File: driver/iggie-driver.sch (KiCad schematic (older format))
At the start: 1 part, among them J101 HV

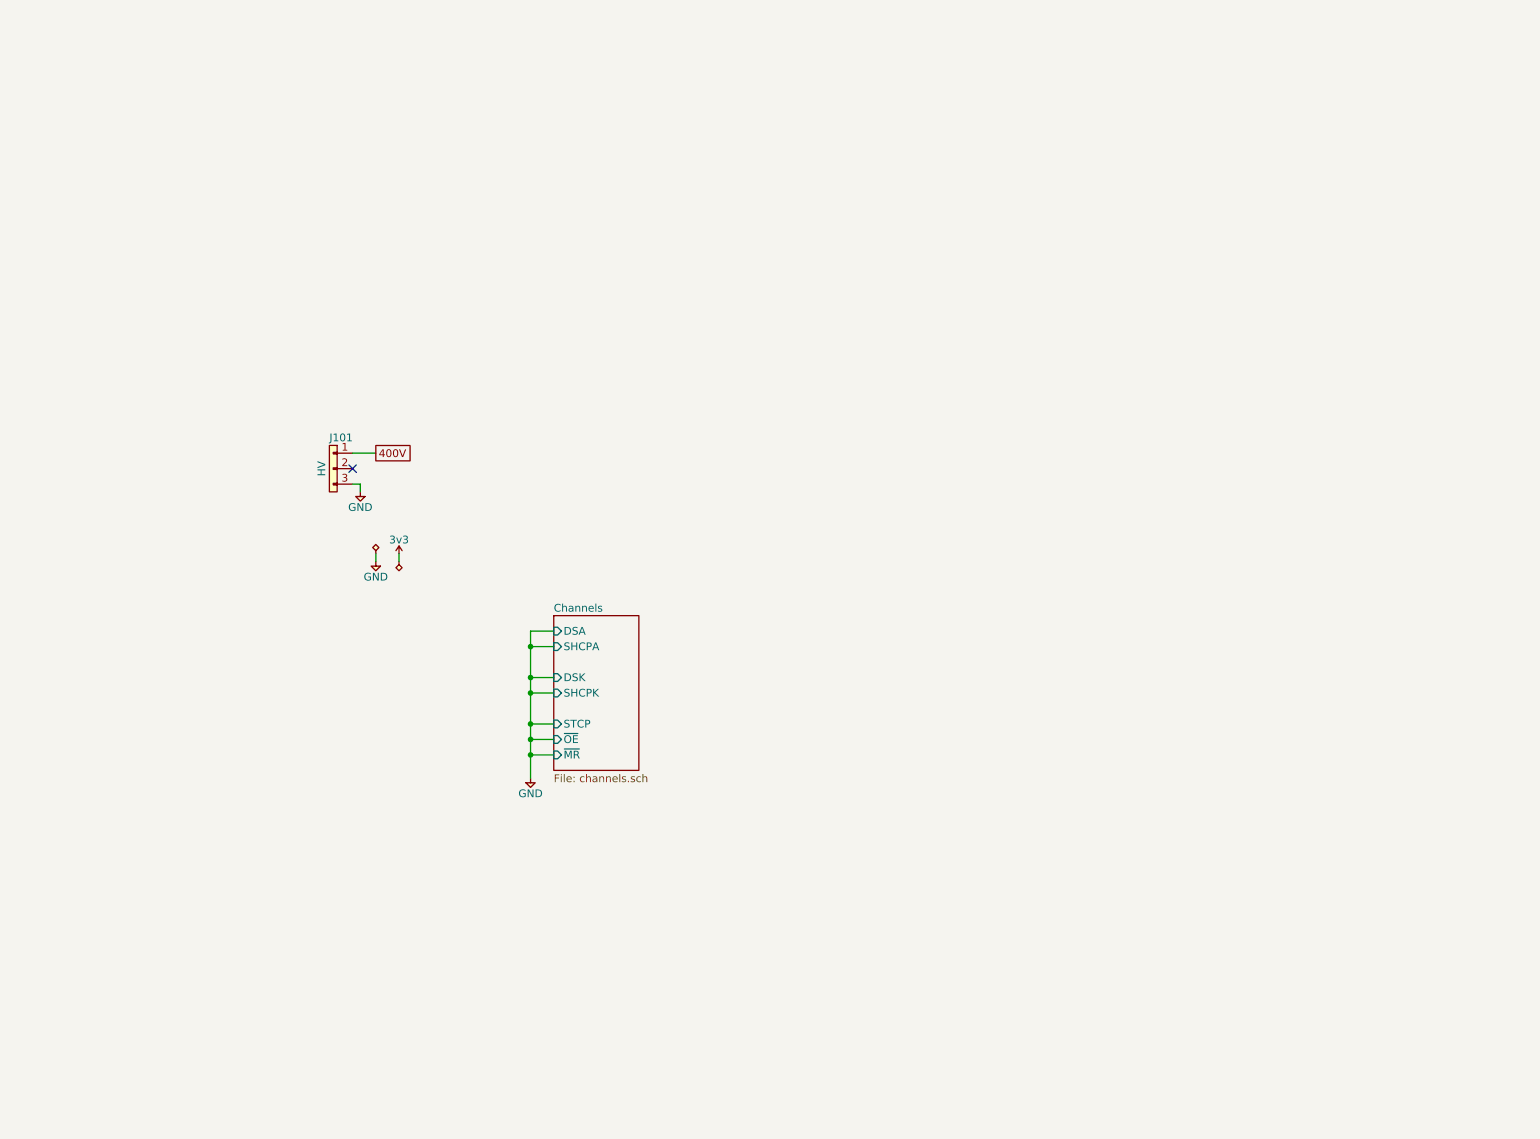
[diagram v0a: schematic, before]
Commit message: Finish sch, start PCB
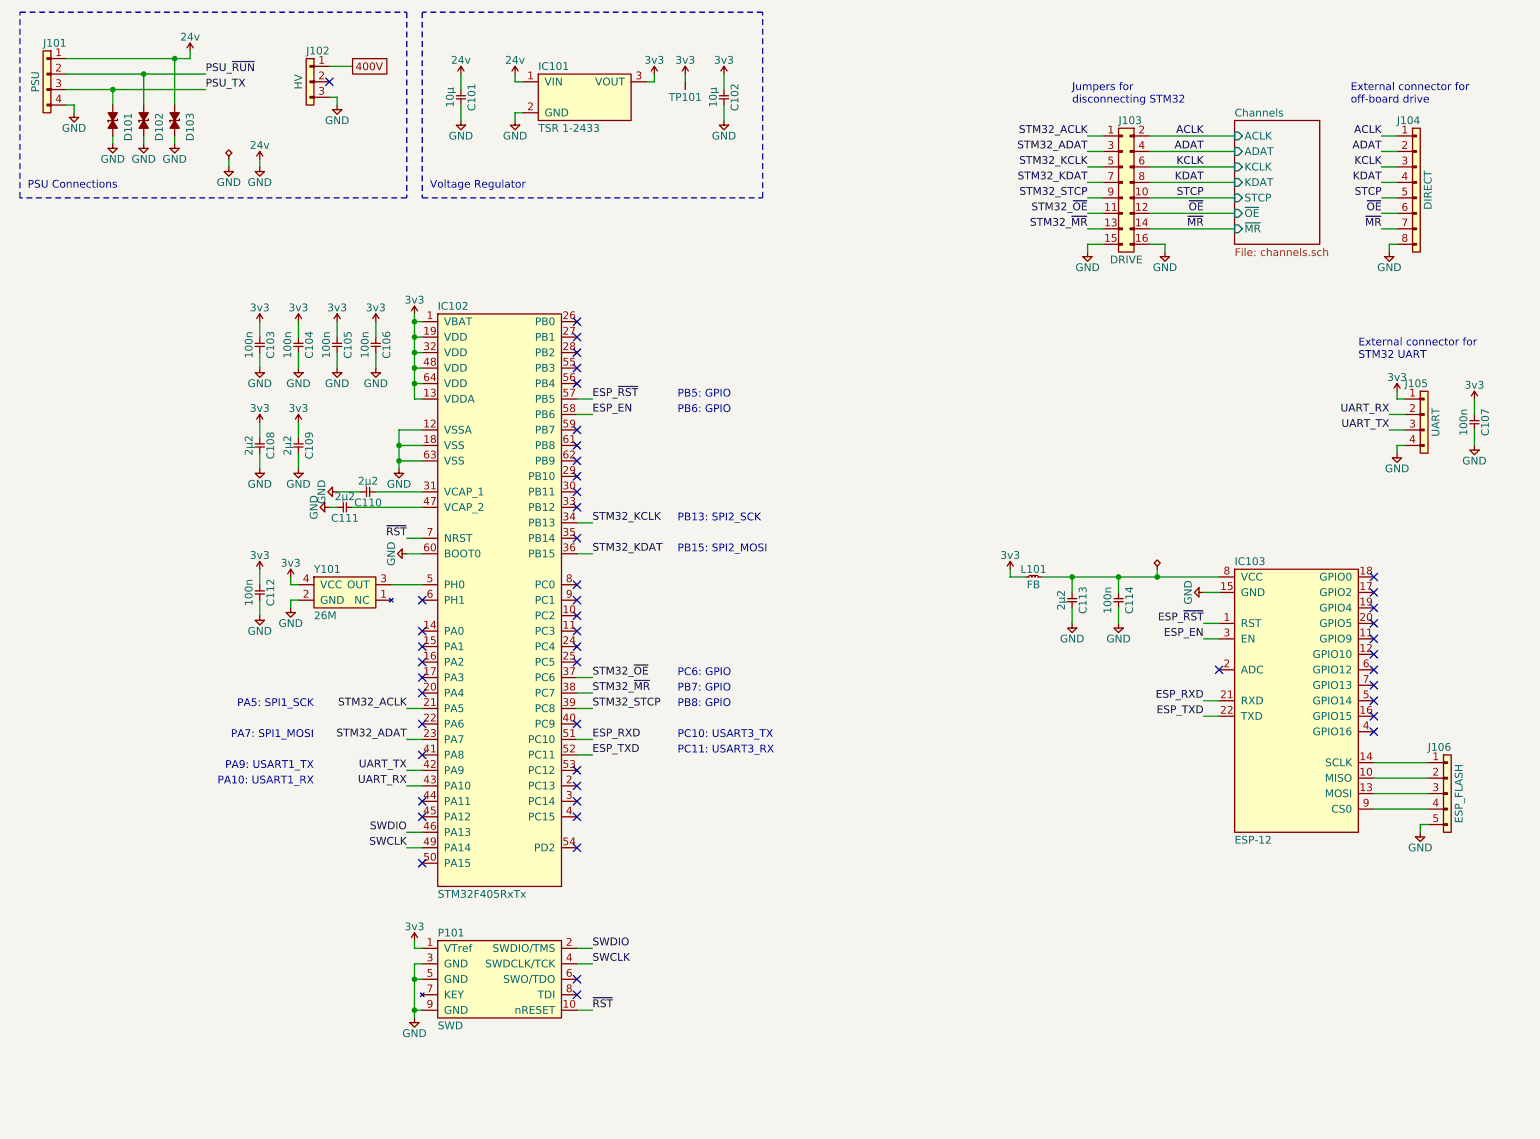
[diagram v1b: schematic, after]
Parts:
- added C101, C102: 10µ, agg:1210, symbol agg-kicad:C
- added C103, C104, C105, C106, C107, C112, C114: 100n, agg:0603, symbol agg-kicad:C
- added C108, C109, C110, C111, C113: 2µ2, agg:0603, symbol agg-kicad:C
- added D101, D102, D103: ESD_DIODE, agg:0603, symbol agg-kicad:ESD_DIODE
- added IC101: TSR 1-2433, agg:TSR1, symbol agg-kicad:TSR1
- added IC102: STM32F405RxTx, agg:LQFP-64, symbol agg-kicad:STM32F405RxTx
- added IC103: ESP-12, agg:ESP-12, symbol agg-kicad:ESP-12
- added J101: PSU, agg:MOLEX-KK-254P-04, symbol agg-kicad:CONN_01x04
- added J103: DRIVE, agg:DIL-254P-16, symbol agg-kicad:CONN_02x08
- added J104: DIRECT, agg:MOLEX-PICOBLADE-53398-0871, symbol agg-kicad:CONN_01x08
- added J105: UART, agg:MOLEX-PICOBLADE-53398-0471, symbol agg-kicad:CONN_01x04
- added J106: ESP_FLASH, agg:SIL-254P-05, symbol agg-kicad:CONN_01x05
- added L101: FB, agg:0603, symbol agg-kicad:L
- added P101: SWD, agg:FTSH-105-01-F-D-K, symbol agg-kicad:SWD
- added TP101: TESTPAD, agg:TESTPAD, symbol agg-kicad:TESTPAD
- added Y101: 26M, agg:XTAL-25x20, symbol agg-kicad:TCXO
- J102: renamed from J101; footprint (none) -> agg:MOLEX-KK-254P-03; Farnell (none) -> 1360131
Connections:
- net 3v3: now also C102.1, C103.1, C104.1, C105.1, C106.1, C107.1, C108.1, C109.1, C112.1, IC101.3 (VOUT), IC102.1 (VBAT), IC102.13 (VDDA), IC102.19 (VDD), IC102.32 (VDD), IC102.48 (VDD), IC102.64 (VDD), J105.1, L101.1, P101.1 (VTref), TP101.1 (TP), Y101.4 (VCC)
- net GND renamed 24v
- net 24v: now also C101.1, C101.2, C102.2, C103.2, C104.2, C105.2, C106.2, C107.2, C108.2, C109.2, C110.2, C111.2, C112.2, C113.2, C114.2, D101.2, D102.2, D103.1, D103.2, IC101.1 (VIN), IC101.2 (GND), IC102.12 (VSSA), IC102.18 (VSS), IC102.60 (BOOT0), IC102.63 (VSS), IC103.15 (GND), J101.1, J101.4, J103.15, J103.16, J104.8, J105.4, J106.5, P101.3 (GND), P101.5 (GND), P101.9 (GND), Y101.2 (GND)
- new net: C110.1, IC102.31 (VCAP_1)
- new net: C111.1, IC102.47 (VCAP_2)
- new net: IC102.5 (PH0), Y101.3 (OUT)
- new net: IC103.10 (MISO), J106.2
- new net: IC103.13 (MOSI), J106.3
- new net: IC103.14 (SCLK), J106.1
- new net: C113.1, C114.1, IC103.8 (VCC), L101.2
- new net: IC103.9 (CS0), J106.4
- new net ACLK: J103.2, J104.1
- new net ADAT: J103.4, J104.2
- new net ESP_EN: IC102.58 (PB6), IC103.3 (EN)
- new net ESP_RXD: IC102.51 (PC10), IC103.21 (RXD)
- new net ESP_TXD: IC102.52 (PC11), IC103.22 (TXD)
- new net ESP_~RST: IC102.57 (PB5), IC103.1 (RST)
- new net KCLK: J103.6, J104.3
- new net KDAT: J103.8, J104.4
- new net PSU_TX: D101.1, J101.3
- new net PSU_~RUN: D102.1, J101.2
- new net STCP: J103.10, J104.5
- new net STM32_ACLK: IC102.21 (PA5), J103.1
- new net STM32_ADAT: IC102.23 (PA7), J103.3
- new net STM32_KCLK: IC102.34 (PB13), J103.5
- new net STM32_KDAT: IC102.36 (PB15), J103.7
- new net STM32_STCP: IC102.39 (PC8), J103.9
- new net STM32_~MR: IC102.38 (PC7), J103.13
- new net STM32_~OE: IC102.37 (PC6), J103.11
- new net SWCLK: IC102.49 (PA14), P101.4 (SWDCLK/TCK)
- new net SWDIO: IC102.46 (PA13), P101.2 (SWDIO/TMS)
- new net UART_RX: IC102.43 (PA10), J105.2
- new net UART_TX: IC102.42 (PA9), J105.3
- new net ~MR: J103.14, J104.7
- new net ~OE: J103.12, J104.6
- new net ~RST: IC102.7 (NRST), P101.10 (nRESET)
- no-connect marks 1 -> 50
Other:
- note added: "External connector for\nSTM32 UART"
- note added: "External connector for\noff-board drive"
- note added: "Jumpers for\ndisconnecting STM32"
- note added: "PA10: USART1_RX"
- note added: "PA5: SPI1_SCK"
- note added: "PA7: SPI1_MOSI"
- note added: "PA9: USART1_TX"
- note added: "PB13: SPI2_SCK"
- note added: "PB15: SPI2_MOSI"
- note added: "PB5: GPIO"
- note added: "PB6: GPIO"
- note added: "PB7: GPIO"
- note added: "PB8: GPIO"
- note added: "PC10: USART3_TX"
- note added: "PC11: USART3_RX"
- note added: "PC6: GPIO"
- note added: "PSU Connections"
- note added: "Voltage Regulator"
- moved on the sheet: J102

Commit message: WIP PCB
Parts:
- added X101, X102, X103, X104, X105, X106, X107, X108: M3 MOUNT, agg:M3_MOUNT, symbol agg-kicad:PART
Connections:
- net 24v: no longer C101.2, C102.2, C103.2, C104.2, C105.2, C106.2, C107.2, C108.2, C109.2, C110.2, C111.2, C112.2, C113.2, C114.2, D101.2, D102.2, D103.2, IC101.2 (GND), IC102.12 (VSSA), IC102.18 (VSS), IC102.60 (BOOT0), IC102.63 (VSS), IC103.15 (GND), J101.4, J102.3, J103.15, J103.16, J104.8, J105.4, J106.5, P101.3 (GND), P101.5 (GND), P101.9 (GND), Y101.2 (GND)
- net 400V: now also J102.3; no longer J102.1
- net at IC103.10 (MISO): now also J106.3; no longer J106.2
- net at IC103.13 (MOSI): now also J106.2; no longer J106.3
- new net GND: C101.2, C102.2, C103.2, C104.2, C105.2, C106.2, C107.2, C108.2, C109.2, C110.2, C111.2, C112.2, C113.2, C114.2, D101.2, D102.2, D103.2, IC101.2 (GND), IC102.12 (VSSA), IC102.18 (VSS), IC102.60 (BOOT0), IC102.63 (VSS), IC103.15 (GND), J101.4, J102.1, J103.15, J103.16, J104.8, J105.4, J106.5, P101.3 (GND), P101.5 (GND), P101.9 (GND), Y101.2 (GND)
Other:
- moved on the sheet: J106
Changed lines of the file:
@@
 Comment4 ""
 $EndDescr
-$Comp
-L agg-kicad:CONN_01x03 J102
-U 1 1 5D894B24
-P 2450 900
-F 0 "J102" H 2400 1000 50  0000 L CNN
-F 1 "HV" V 2350 800 50  0000 C CNN
-F 2 "agg:MOLEX-KK-254P-03" H 2450 900 50  0001 C CNN
-F 3 "" H 2450 900 50  0001 C CNN
-F 4 "1360131" H 2450 900 50  0001 C CNN "Farnell"
-	1    2450 900
-	1    0    0    -1
-$EndComp
 NoConn ~ 2550 1000
 $Comp
@@
 	1    2100 1500
 	1    0    0    -1
-$EndComp
-$Comp
-L agg-kicad:GND #PWR0117
-U 1 1 8382BEE8
-P 2100 1550
-F 0 "#PWR0117" H 1970 1590 50  0001 L CNN
-F 1 "GND" H 2100 1450 50  0000 C CNN
-F 2 "" H 2100 1550 50  0001 C CNN
-F 3 "" H 2100 1550 50  0001 C CNN
-	1    2100 1550
-	-1   0    0    -1
 $EndComp
 Wire Wire Line
@@
 	1    0    0    -1
 $EndComp
-$Comp
-L agg-kicad:CONN_01x05 J106
-U 1 1 83A0715A
-P 9750 5400
-F 0 "J106" H 9700 5500 50  0000 L CNN
-F 1 "ESP_FLASH" V 9650 5200 50  0000 C CNN
-F 2 "agg:SIL-254P-05" H 9750 5400 50  0001 C CNN
-F 3 "" H 9750 5400 50  0001 C CNN
-	1    9750 5400
-	-1   0    0    -1
-$EndComp
-Wire Wire Line
-	9300 5400 9650 5400
-Wire Wire Line
-	9650 5500 9300 5500
-Wire Wire Line
-	9300 5600 9650 5600
-Wire Wire Line
-	9650 5700 9300 5700
-$Comp
-L agg-kicad:GND #PWR0150
-U 1 1 83A1A036
-P 9600 5850
-F 0 "#PWR0150" H 9470 5890 50  0001 L CNN
-F 1 "GND" H 9600 5750 50  0000 C CNN
-F 2 "" H 9600 5850 50  0001 C CNN
-F 3 "" H 9600 5850 50  0001 C CNN
-	1    9600 5850
-	1    0    0    -1
-$EndComp
-Wire Wire Line
-	9600 5850 9600 5800
-Wire Wire Line
-	9600 5800 9650 5800
 Wire Wire Line
 	8300 5000 8200 5000
@@
 Wire Wire Line
 	7900 4200 8300 4200
+$Comp
+L agg-kicad:PART X105
+U 1 1 83D5BB64
+P 500 7700
+F 0 "X105" H 550 7800 50  0000 L CNN
+F 1 "M3 MOUNT" H 550 7700 50  0000 L CNN
+F 2 "agg:M3_MOUNT" H 500 7700 50  0001 C CNN
+F 3 "" H 500 7700 50  0001 C CNN
+	1    500  7700
+	1    0    0    -1
+$EndComp
+$Comp
+L agg-kicad:PART X106
+U 1 1 83D5F3E2
+P 1050 7700
+F 0 "X106" H 1100 7800 50  0000 L CNN
+F 1 "M3 MOUNT" H 1100 7700 50  0000 L CNN
+F 2 "agg:M3_MOUNT" H 1050 7700 50  0001 C CNN
+F 3 "" H 1050 7700 50  0001 C CNN
+	1    1050 7700
+	1    0    0    -1
+$EndComp
+$Comp
+L agg-kicad:PART X107
+U 1 1 83D5F6EB
+P 1600 7700
+F 0 "X107" H 1650 7800 50  0000 L CNN
+F 1 "M3 MOUNT" H 1650 7700 50  0000 L CNN
+F 2 "agg:M3_MOUNT" H 1600 7700 50  0001 C CNN
+F 3 "" H 1600 7700 50  0001 C CNN
+	1    1600 7700
+	1    0    0    -1
+$EndComp
+$Comp
+L agg-kicad:PART X108
+U 1 1 83D5FB17
+P 2150 7700
+F 0 "X108" H 2200 7800 50  0000 L CNN
+F 1 "M3 MOUNT" H 2200 7700 50  0000 L CNN
+F 2 "agg:M3_MOUNT" H 2150 7700 50  0001 C CNN
+F 3 "" H 2150 7700 50  0001 C CNN
+	1    2150 7700
+	1    0    0    -1
+$EndComp
+$Comp
+L agg-kicad:PART X104
+U 1 1 83D5FDE9
+P 2150 7450
+F 0 "X104" H 2200 7550 50  0000 L CNN
+F 1 "M3 MOUNT" H 2200 7450 50  0000 L CNN
+F 2 "agg:M3_MOUNT" H 2150 7450 50  0001 C CNN
+F 3 "" H 2150 7450 50  0001 C CNN
+	1    2150 7450
+	1    0    0    -1
+$EndComp
+$Comp
+L agg-kicad:PART X103
+U 1 1 83D600CB
+P 1600 7450
+F 0 "X103" H 1650 7550 50  0000 L CNN
+F 1 "M3 MOUNT" H 1650 7450 50  0000 L CNN
+F 2 "agg:M3_MOUNT" H 1600 7450 50  0001 C CNN
+F 3 "" H 1600 7450 50  0001 C CNN
+	1    1600 7450
+	1    0    0    -1
+$EndComp
+$Comp
+L agg-kicad:PART X102
+U 1 1 83D6036C
+P 1050 7450
+F 0 "X102" H 1100 7550 50  0000 L CNN
+F 1 "M3 MOUNT" H 1100 7450 50  0000 L CNN
+F 2 "agg:M3_MOUNT" H 1050 7450 50  0001 C CNN
+F 3 "" H 1050 7450 50  0001 C CNN
+	1    1050 7450
+	1    0    0    -1
+$EndComp
+$Comp
+L agg-kicad:PART X101
+U 1 1 83D606DD
+P 500 7450
+F 0 "X101" H 550 7550 50  0000 L CNN
+F 1 "M3 MOUNT" H 550 7450 50  0000 L CNN
+F 2 "agg:M3_MOUNT" H 500 7450 50  0001 C CNN
+F 3 "" H 500 7450 50  0001 C CNN
+	1    500  7450
+	1    0    0    -1
+$EndComp
+$Comp
+L agg-kicad:PWR #FLG0103
+U 1 1 83D6639C
+P 2100 1550
+F 0 "#FLG0103" H 2100 1710 50  0001 C CNN
+F 1 "PWR" H 2100 1640 50  0001 C CNN
+F 2 "" H 2100 1550 50  0001 C CNN
+F 3 "" H 2100 1550 50  0001 C CNN
+	1    2100 1550
+	-1   0    0    1
+$EndComp
+$Comp
+L agg-kicad:CONN_01x03 J102
+U 1 1 5D894B24
+P 2450 1100
+F 0 "J102" H 2300 800 50  0000 L CNN
+F 1 "HV" V 2350 1000 50  0000 C CNN
+F 2 "agg:MOLEX-KK-254P-03" H 2450 1100 50  0001 C CNN
+F 3 "" H 2450 1100 50  0001 C CNN
+F 4 "1360131" H 2450 1100 50  0001 C CNN "Farnell"
+	1    2450 1100
+	1    0    0    1
+$EndComp
+$Comp
+L agg-kicad:CONN_01x05 J106
+U 1 1 83A0715A
+P 10000 5400
+F 0 "J106" H 9950 5500 50  0000 L CNN
+F 1 "ESP_FLASH" V 9900 5200 50  0000 C CNN
+F 2 "agg:SIL-254P-05" H 10000 5400 50  0001 C CNN
+F 3 "" H 10000 5400 50  0001 C CNN
+	1    10000 5400
+	-1   0    0    -1
+$EndComp
+Wire Wire Line
+	9300 5400 9900 5400
+Wire Wire Line
+	9900 5700 9300 5700
+$Comp
+L agg-kicad:GND #PWR0150
+U 1 1 83A1A036
+P 9850 5850
+F 0 "#PWR0150" H 9720 5890 50  0001 L CNN
+F 1 "GND" H 9850 5750 50  0000 C CNN
+F 2 "" H 9850 5850 50  0001 C CNN
+F 3 "" H 9850 5850 50  0001 C CNN
+	1    9850 5850
+	1    0    0    -1
+$EndComp
+Wire Wire Line
+	9850 5850 9850 5800
+Wire Wire Line
+	9850 5800 9900 5800
+Wire Wire Line
+	9300 5600 9600 5600
+Wire Wire Line
+	9600 5600 9600 5500
+Wire Wire Line
+	9600 5500 9900 5500
+Wire Wire Line
+	9300 5500 9450 5500
+Wire Wire Line
+	9450 5500 9450 5800
+Wire Wire Line
+	9450 5800 9750 5800
+Wire Wire Line
+	9750 5800 9750 5600
+Wire Wire Line
+	9750 5600 9900 5600
 $EndSCHEMATC
